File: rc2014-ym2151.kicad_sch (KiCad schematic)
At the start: 27 parts, among them CON1 SJ1-3523N, J1 Conn_01x03, P1 RC2014 BUS, U1 74HCT688, U2 YM2151, U3 YM3012, U4 NJM4556, U5 NJM4556, X1 3.579545MHz

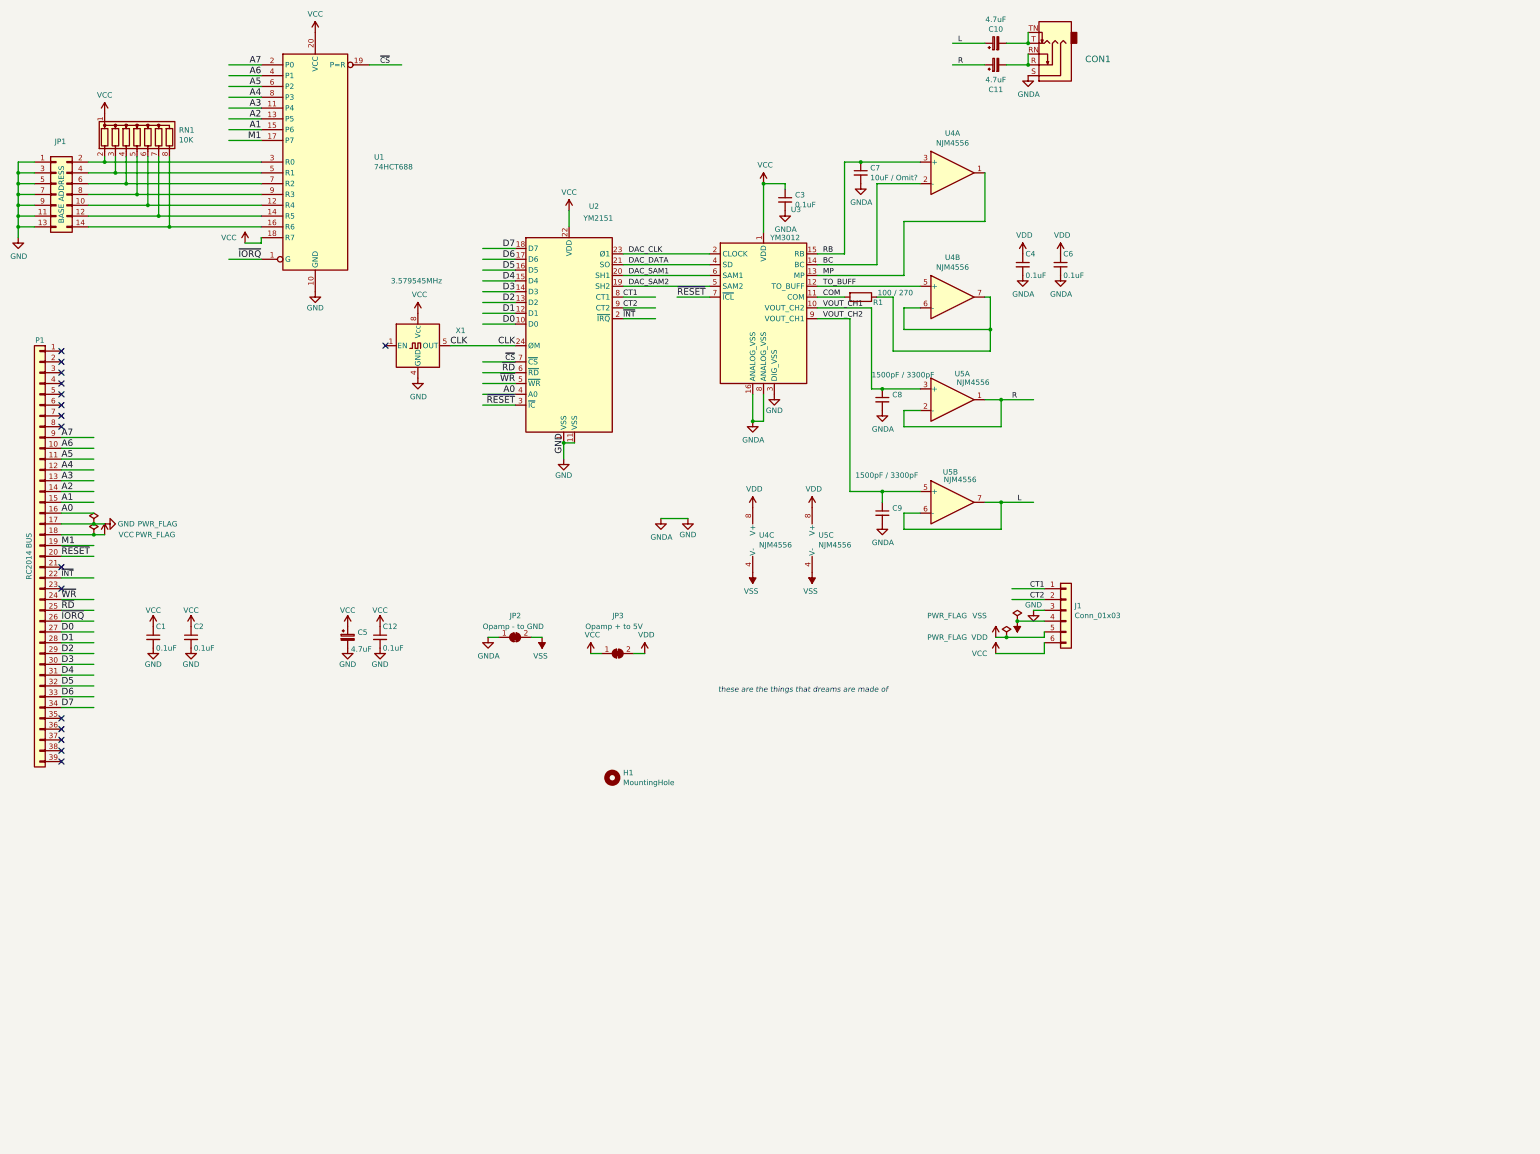
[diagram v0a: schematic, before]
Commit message: Tidy up schematic further
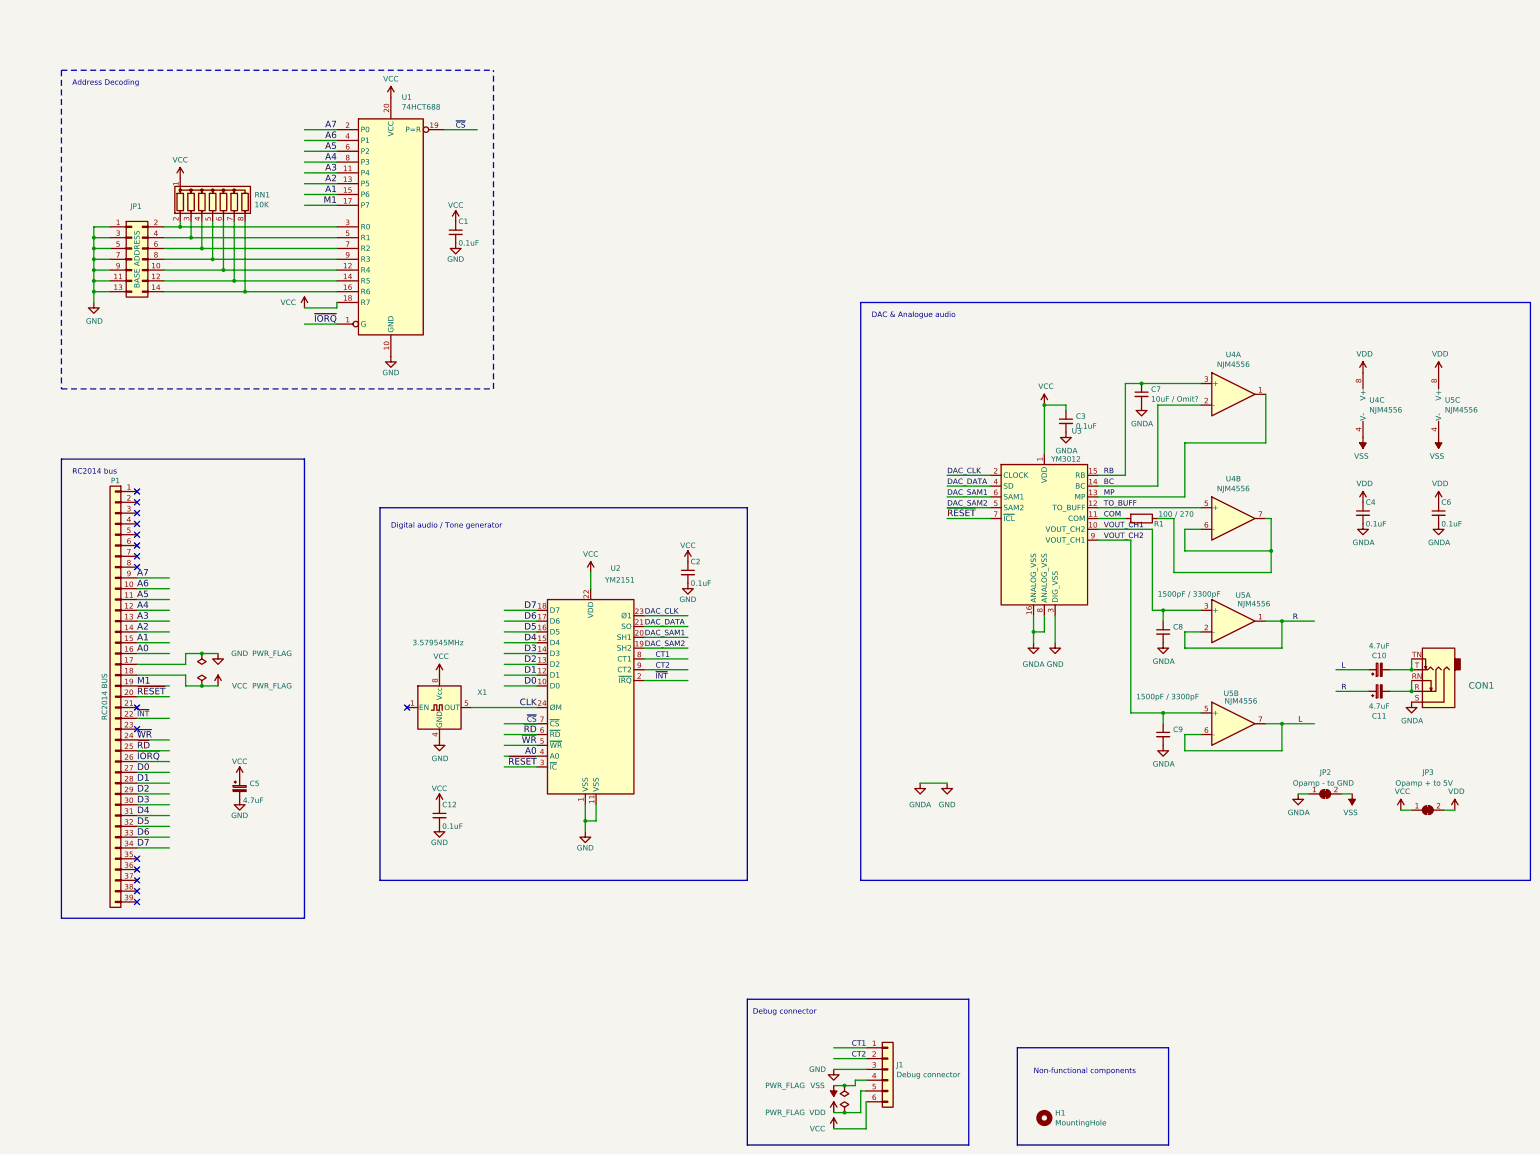
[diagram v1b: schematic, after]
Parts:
- J1: value Conn_01x03 -> Debug connector
- U2: footprint Package_DIP:DIP-24_W15.24mm -> Package_DIP:DIP-24_W15.24mm_Socket
- U3: footprint Package_DIP:DIP-16_W7.62mm -> Package_DIP:DIP-16_W7.62mm_Socket
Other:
- note added: "Address Decoding"
- note added: "DAC & Analogue audio"
- note added: "Debug connector"
- note added: "Digital audio / Tone generator"
- note added: "Non-functional components"
- note added: "RC2014 bus"
- note removed: "these are the things that dreams are made of"
- moved on the sheet: C1, C10, C11, C12, C2, C3, C4, C5, C6, C7, C8, C9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

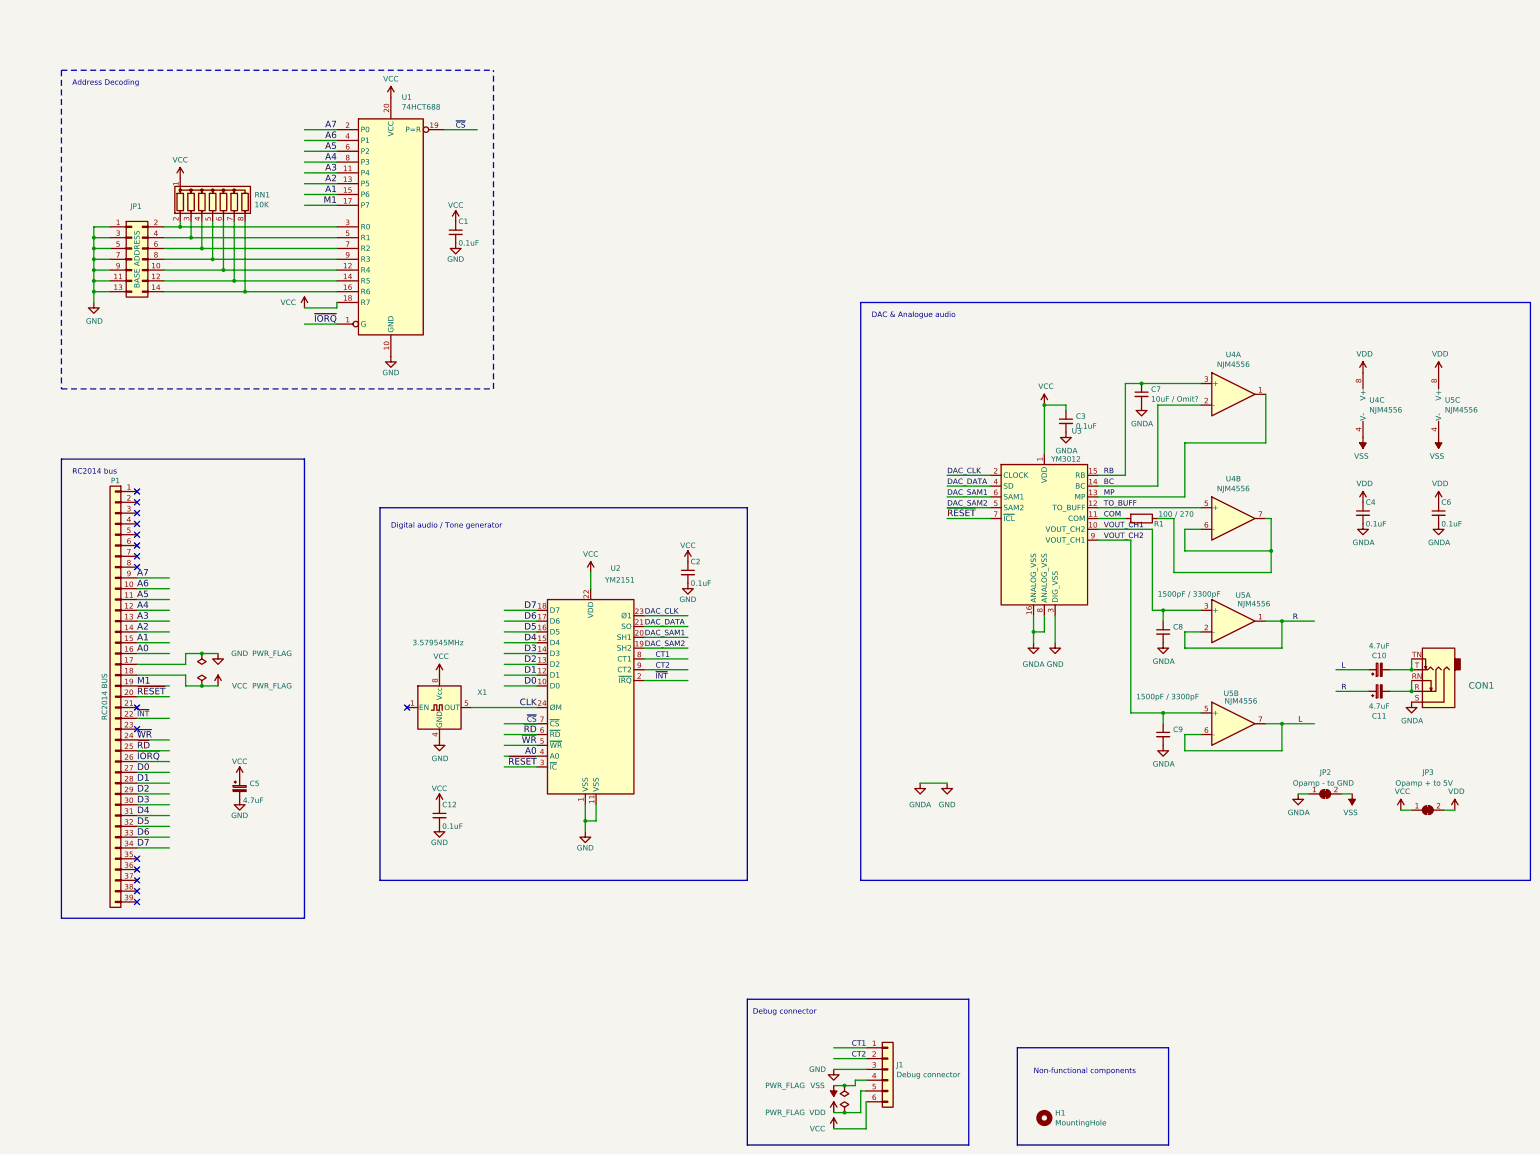
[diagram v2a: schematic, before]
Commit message: migrate to kicad 9 - fix most of the ERC and DRC issues, use current library symbols/footprints
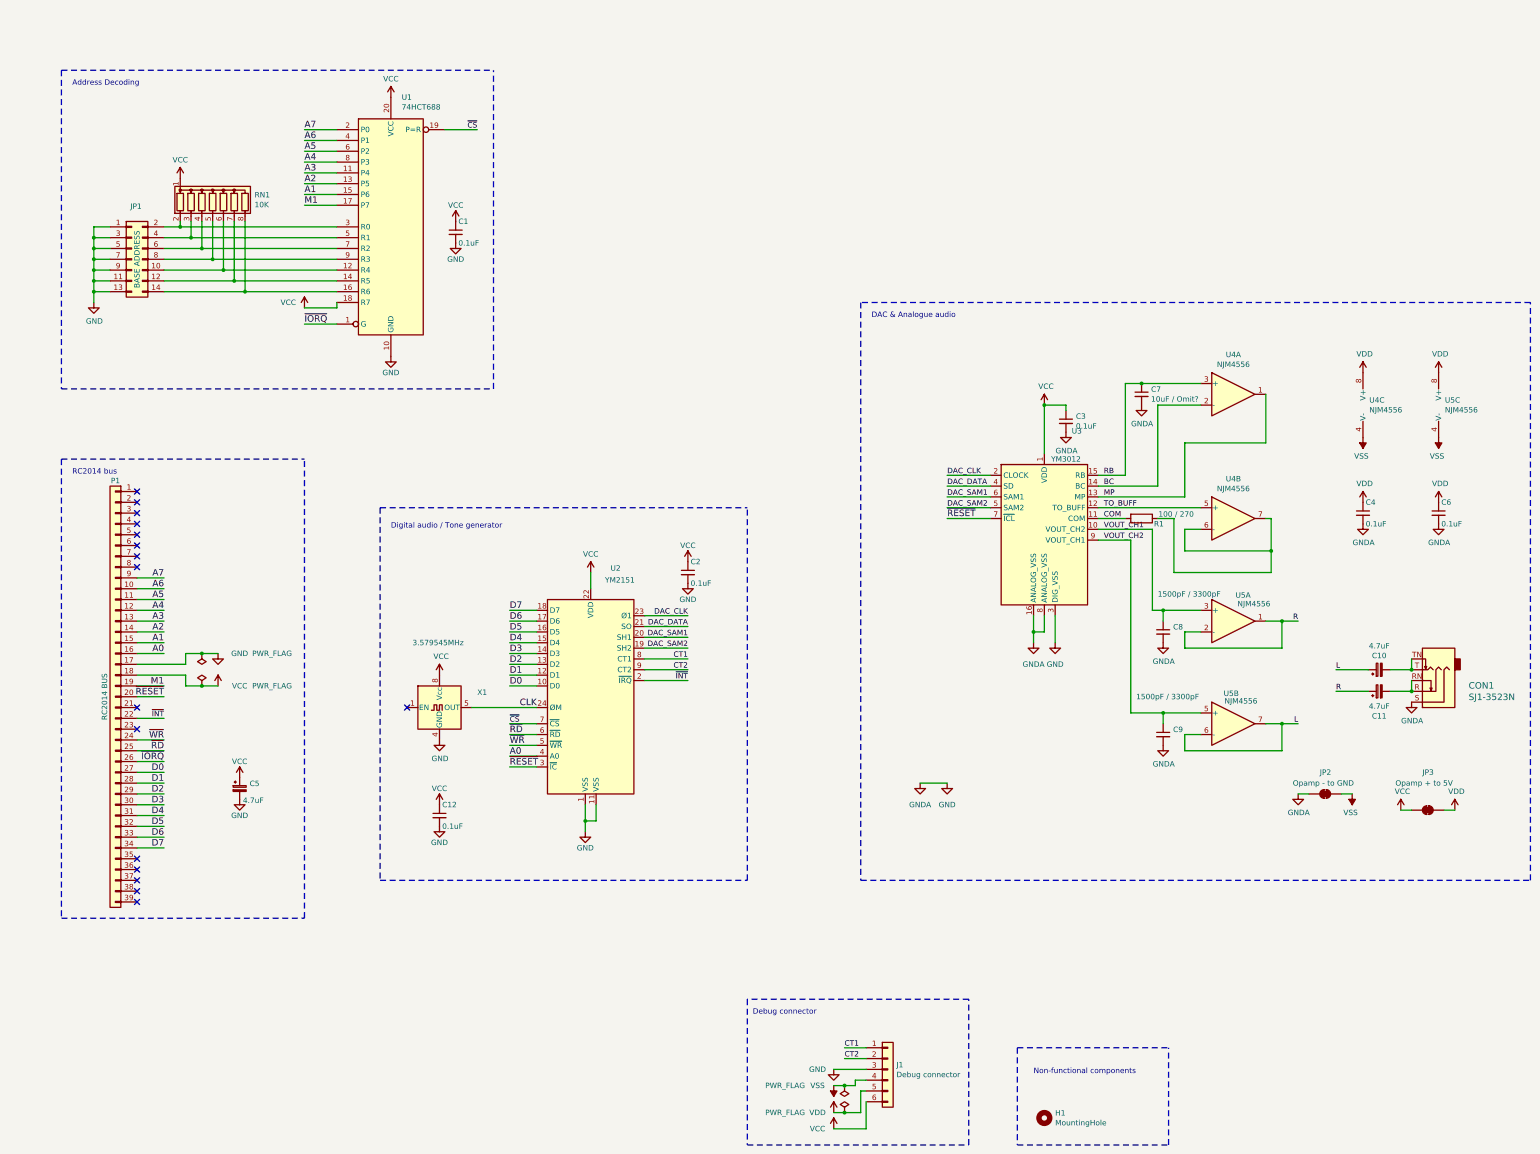
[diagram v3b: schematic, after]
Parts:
- CON1: symbol Connector:AudioJack3_SwitchTR -> Connector_Audio:AudioJack3_SwitchTR
- U2: footprint Package_DIP:DIP-24_W15.24mm_Socket -> Package_DIP:DIP-24_W15.24mm
- U3: footprint Package_DIP:DIP-16_W7.62mm_Socket -> Package_DIP:DIP-16_W7.62mm
